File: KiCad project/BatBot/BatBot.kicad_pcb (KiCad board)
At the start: 4 copper layers, 56 parts, among them J1 54550-1271, U1 STM32F439ZIYx, U2 nRF24L01P, U3 MPU-9250, U4 LM1117MPX-3_3_NOPB, X1 NX3225GD-8MHZ-STD-CRA-3, X2 XRCHA16M000F0A01R0

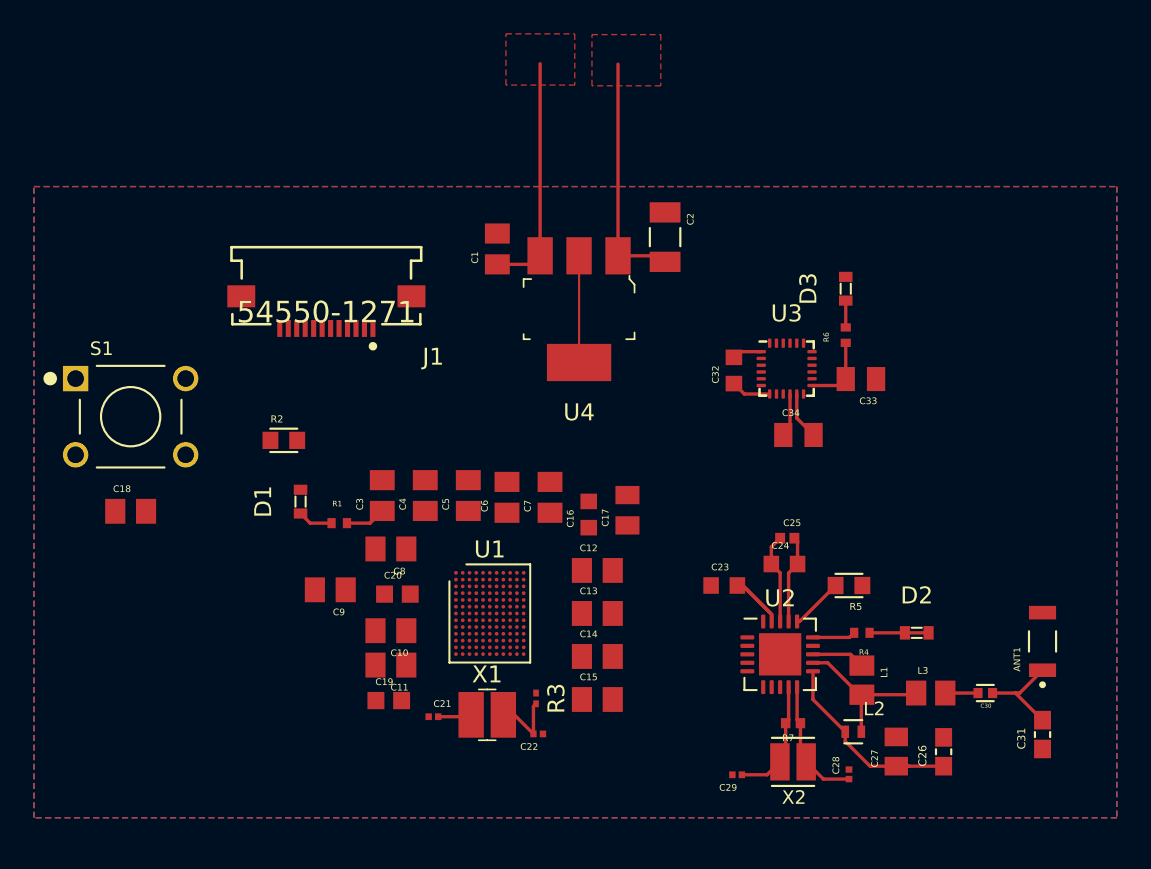
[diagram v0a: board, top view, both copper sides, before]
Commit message: finished draft board design, updated schematic
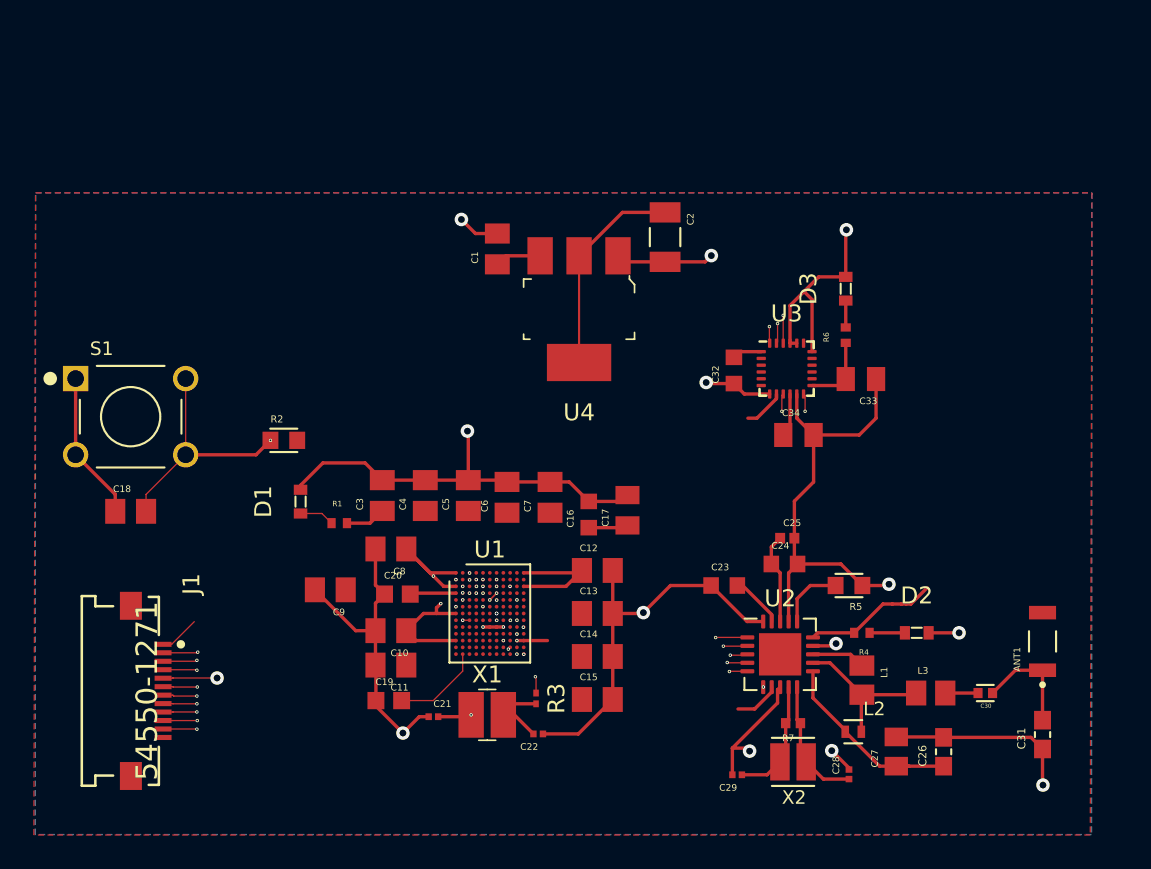
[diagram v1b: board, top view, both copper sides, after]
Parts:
- moved J1 24.7 mm to (102.2, 110.0), turned to 270 degrees
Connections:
- C10 pad 2: Net-(C10-Pad2) -> GND
- C11 pad 2: Net-(C10-Pad2) -> GND
- C12 pad 2: Net-(C10-Pad2) -> GND
- C13 pad 2: Net-(C10-Pad2) -> GND
- C14 pad 2: Net-(C10-Pad2) -> GND
- C15 pad 2: Net-(C10-Pad2) -> GND
- J1 pad 11: JTDI -> JTCK-SWCLK
- U1 pad C2: JTDI -> JTCK-SWCLK
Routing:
- net GND: track 24.7 -> 153.9 mm, vias 0 -> 22
- net JTCK-SWCLK: track 0.00 -> 72.0 mm, vias 0 -> 4
- net NJTRST: track 0.00 -> 64.5 mm, vias 0 -> 2
- net JTDO-SWO: track 0.00 -> 58.7 mm, vias 0 -> 2
- net +3V3: track 22.6 -> 77.4 mm, vias 0 -> 11
- net SPI1-SCLK: track 0.00 -> 48.9 mm, vias 0 -> 3
- net SPI1-MOSI: track 0.00 -> 41.5 mm, vias 0 -> 6
- net Net-(C18-Pad2): track 0.00 -> 39.9 mm, vias 0 -> 2
- net SPI1-MISO: track 0.00 -> 34.9 mm, vias 0 -> 8
- net IMU_CS: track 0.00 -> 29.5 mm, vias 0 -> 3
- net IMU_INT: track 0.00 -> 28.4 mm, vias 0 -> 4
- net NRF_CS: track 0.00 -> 24.0 mm, vias 0 -> 3
- net USART1-RX: track 0.00 -> 23.2 mm, vias 0 -> 2
- net USART1-CTS: track 0.00 -> 22.1 mm, vias 0 -> 2
- net JTMS-SWDIO: track 0.00 -> 21.2 mm, vias 0 -> 2
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- removed copper zone on F.Cu, net GND
- removed copper zone on F.Cu, net Net-(C1-Pad1)
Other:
- net class Default: clearance 0.2 -> 0.1; trace_width 0.127 -> 0.0762
- rule trace_clearance: 0.2 -> 0.1
- rule trace_min: 0.05 -> 0.01

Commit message: fix all DRC errors, swap microvias to blind/burried/through
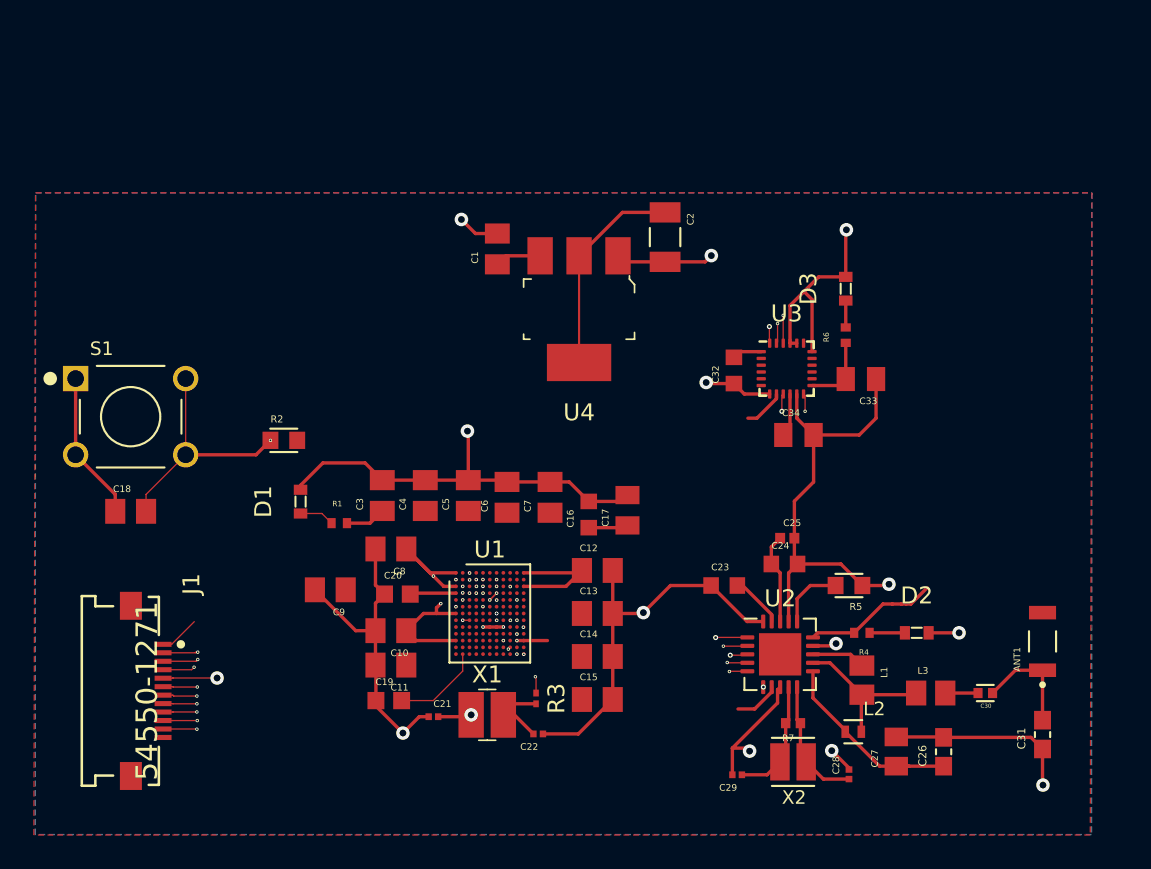
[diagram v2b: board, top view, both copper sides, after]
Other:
- rule trace_min: 0.01 -> 0.0762
- rule via_min_drill: 0.3 -> 0.1
- rule via_min_size: 0.4 -> 0.2

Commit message: update vias/traces to match PCB way requirements
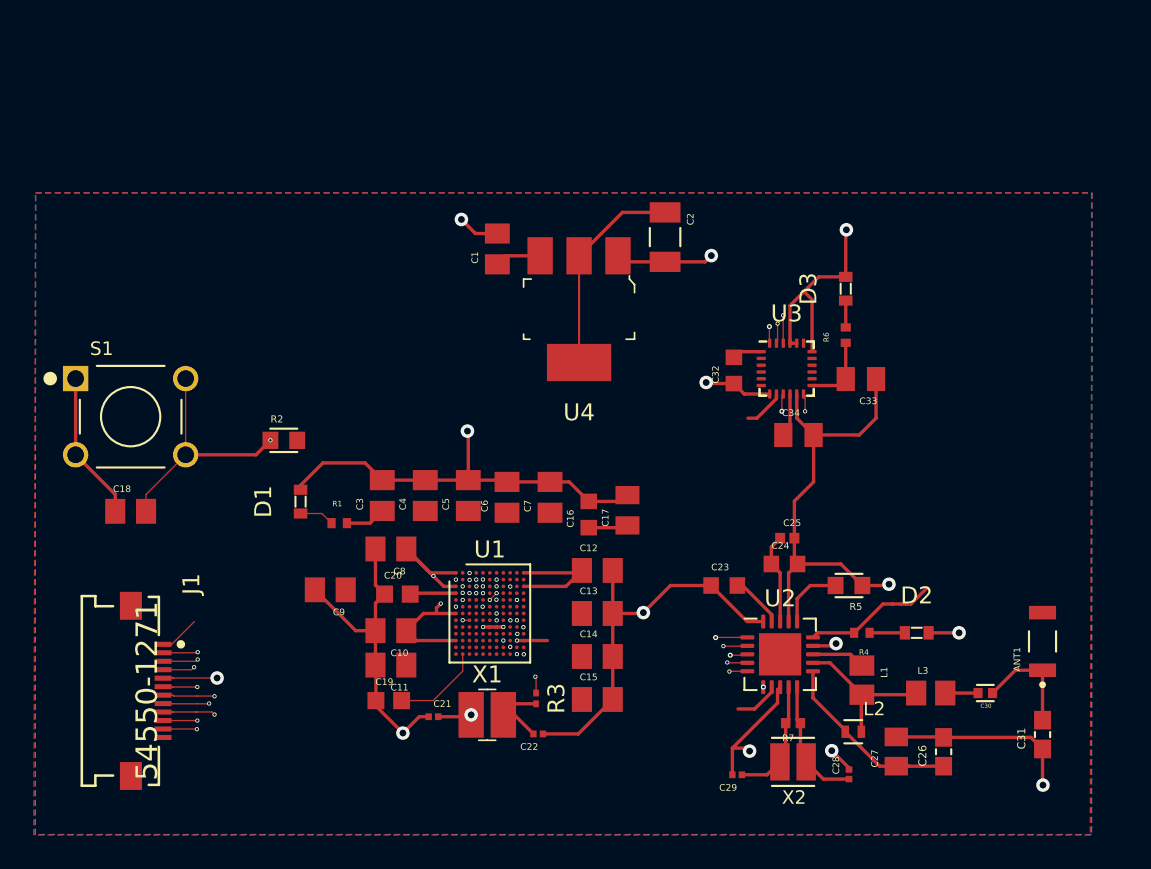
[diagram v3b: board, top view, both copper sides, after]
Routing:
- net IMU_CS: track 29.5 -> 34.2 mm
- net SPI1-MOSI: track 41.5 -> 43.5 mm
- net NJTRST: track 64.5 -> 63.6 mm
- net +3V3: vias 11 -> 10
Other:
- rule via_min_drill: 0.1 -> 0.15
- rule via_min_size: 0.2 -> 0.25
